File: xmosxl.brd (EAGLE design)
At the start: 130 x 85 mm, 139 parts, among them IC1 74LVC1T45W6-7, IC2 74LVC1T45W6-7, IC3 74LVC1T45W6-7, IC4 74LVC1T45W6-7, IC5 74LVC1T45W6-7, IC6 74ALVC164245DGG_11, IC7 74ALVC164245DGG_11, IC8 74LVC1T45W6-7, IC9 74LVC1T45W6-7, U1 24 MHz Osc. (F535L-24)

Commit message: Dd the link resistors
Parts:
- added R31, R32, R33, R34, R35: 33R, rcl:R0201
- moved R28 6.71 mm to (82.0, 52.5), turned to 180 degrees
- moved R16 6.40 mm to (79.0, 46.5)
- moved R17 6.02 mm to (77.5, 46.5)
- moved C39 1.50 mm to (67.0, 46.5)
- moved R24 1.00 mm to (53.5, 68.5)
- moved C27 0.50 mm to (65.0, 46.5)
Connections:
- new net N$27: R31.1, XMOS.N2
- new net N$28: R32.1, XMOS.P2
- new net N$29: R34.1, XMOS.R1
- new net N$30: R35.1, XMOS.R2
- net +5V: no longer JP1.13
- net RX0: no longer JP1.5
- net RX1: now also JP1.5; no longer JP1.9
- net RX2: now also JP1.9
- net RX3: now also JP1.13
- net RX4: now also R33.1
- net TX0: now also R31.2
- net TX1: now also R32.2
- net TX2: now also R33.2
- net TX3: now also R34.2
- net TX4: now also R35.2

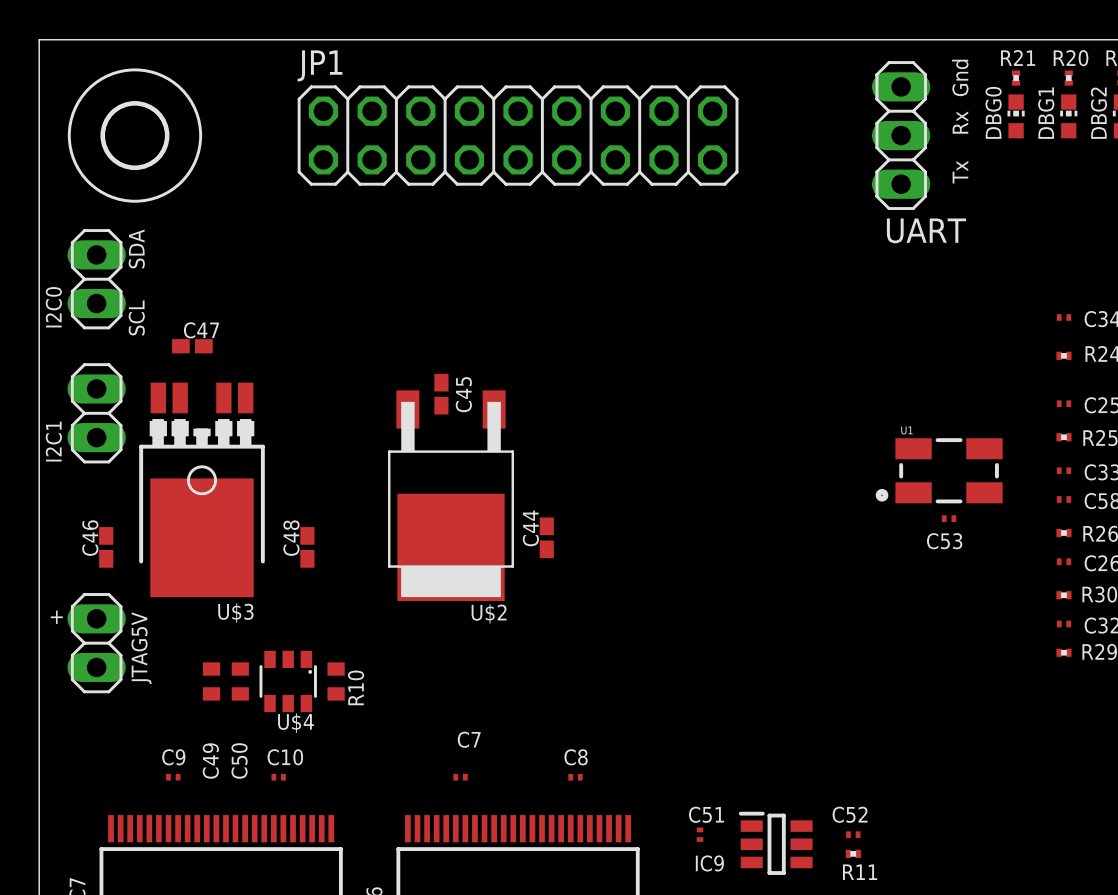
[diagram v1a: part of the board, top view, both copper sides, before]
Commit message: Board circuit-complete. Decided to ditch the SPI expansion.
Need to set signal classes and routing hints
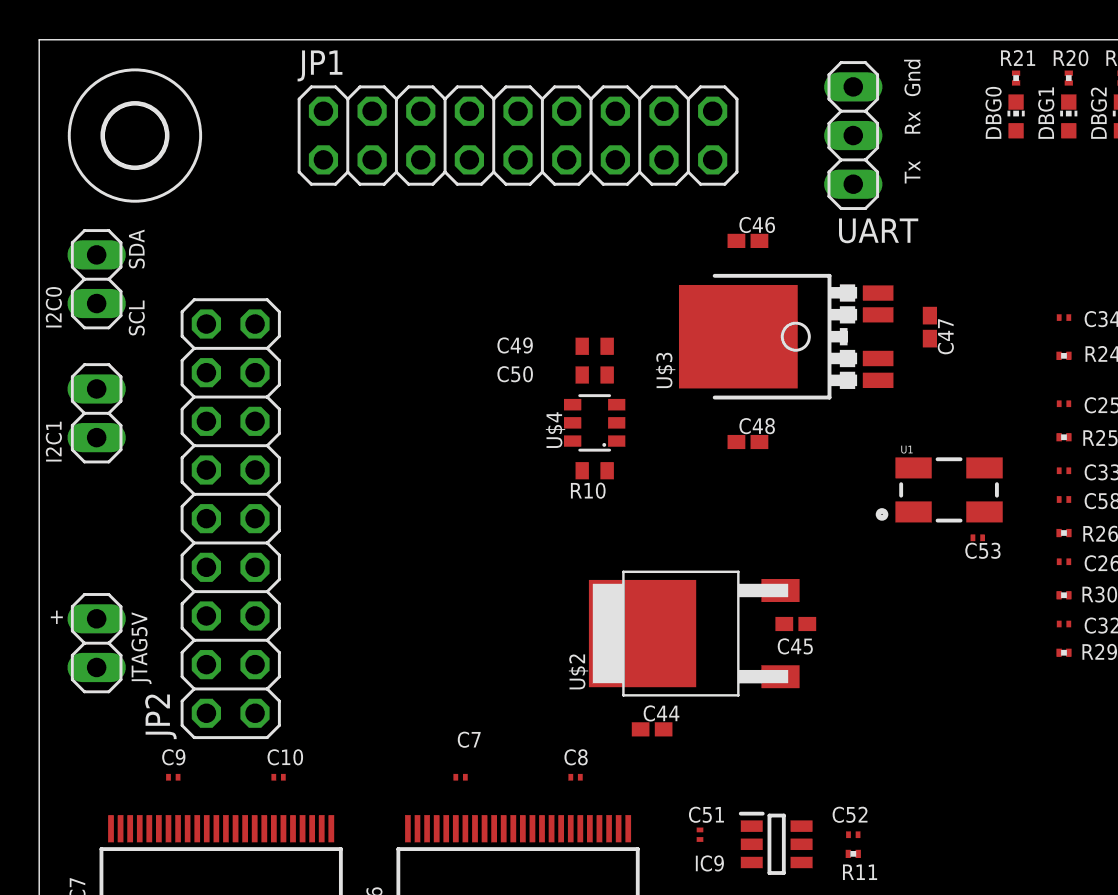
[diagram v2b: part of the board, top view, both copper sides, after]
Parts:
- added JP2: (no value), pinhead:2X09
- moved C47 38.5 mm to (46.5, 70.0), turned to 270 degrees
- moved C46 37.1 mm to (37.0, 74.5), turned to 0 degrees
- moved U$3 31.5 mm to (39.0, 69.5), turned to 90 degrees
- moved C49 26.6 mm to (29.0, 69.0), turned to 0 degrees
- moved C50 24.5 mm to (29.0, 67.5), turned to 0 degrees
- moved C48 23.6 mm to (37.0, 64.0), turned to 0 degrees
- moved C45 22.1 mm to (39.5, 54.5), turned to 0 degrees
- moved U$4 20.9 mm to (29.0, 65.0), turned to 90 degrees
- moved R10 17.4 mm to (29.0, 62.5), turned to 180 degrees
- moved C44 11.4 mm to (32.0, 49.0), turned to 0 degrees
- moved U$2 11.0 mm to (31.5, 54.0), turned to 90 degrees
- moved UART 2.50 mm to (42.5, 80.0)
- moved C53 1.80 mm to (49.0, 59.0)
- moved U1 1.00 mm to (47.5, 61.5)
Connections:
- new net XPND_CTRL0: JP2.3, XMOS.D19
- new net XPND_CTRL1: JP2.5, XMOS.D20
- new net XPND_CTRL2: JP2.7, XMOS.C13
- new net XPND_CTRL3: JP2.9, XMOS.D13
- new net XPND_CTRL4: JP2.11, XMOS.AA12
- new net XPND_CTRL5: JP2.13, XMOS.Y15
- new net XPND_CTRL6: JP2.15, XMOS.Y19
- new net XPND_DATA0: JP2.2, XMOS.U21
- new net XPND_DATA1: JP2.4, XMOS.T21
- new net XPND_DATA2: JP2.6, XMOS.R20
- new net XPND_DATA3: JP2.8, XMOS.R21
- new net XPND_DATA4: JP2.10, XMOS.P20
- new net XPND_DATA5: JP2.12, XMOS.P21
- new net XPND_DATA6: JP2.14, XMOS.E20
- new net XPND_DATA7: JP2.16, XMOS.E21
- net +3V3: now also SLOT1.B16, SLOT2.B17, SLOT3.B16, SLOT3.B17, SLOT4.B18, SLOT5.B16, SLOT5.B18; no longer JP1.11, JP1.12
- net +5V: now also JP1.3, JP1.4, JP2.1, SLOT1.A1, SLOT1.A2, SLOT1.B1, SLOT1.B2, SLOT2.A1, SLOT2.A2, SLOT2.B1, SLOT2.B2, SLOT3.A1, SLOT3.A2, SLOT3.B1, SLOT3.B2, SLOT4.A1, SLOT4.A2, SLOT4.B1, SLOT4.B2, SLOT5.A1, SLOT5.A2, SLOT5.B1, SLOT5.B2
- net GND: now also JP1.11, JP1.12, JP1.15, JP1.16, JP2.17, JP2.18, SLOT1.B17, SLOT1.B18, SLOT1.B19, SLOT1.B20, SLOT1.B21, SLOT1.B22, SLOT1.B23, SLOT1.B24, SLOT1.B25, SLOT1.B26, SLOT1.B27, SLOT1.B28, SLOT1.B29, SLOT1.B30, SLOT1.B31, SLOT1.B32, SLOT2.B16, SLOT2.B18, SLOT2.B19, SLOT2.B20, SLOT2.B21, SLOT2.B22, SLOT2.B23, SLOT2.B24, SLOT2.B25, SLOT2.B26, SLOT2.B27, SLOT2.B28, SLOT2.B29, SLOT2.B30, SLOT2.B31, SLOT2.B32, SLOT3.B18, SLOT3.B19, SLOT3.B20, SLOT3.B21, SLOT3.B22, SLOT3.B23, SLOT3.B24, SLOT3.B25, SLOT3.B26, SLOT3.B27, SLOT3.B28, SLOT3.B29, SLOT3.B30, SLOT3.B31, SLOT3.B32, SLOT4.B16, SLOT4.B17, SLOT4.B19, SLOT4.B20, SLOT4.B21, SLOT4.B22, SLOT4.B23, SLOT4.B24, SLOT4.B25, SLOT4.B26, SLOT4.B27, SLOT4.B28, SLOT4.B29, SLOT4.B30, SLOT4.B31, SLOT4.B32, SLOT5.B17, SLOT5.B19, SLOT5.B20, SLOT5.B21, SLOT5.B22, SLOT5.B23, SLOT5.B24, SLOT5.B25, SLOT5.B26, SLOT5.B27, SLOT5.B28, SLOT5.B29, SLOT5.B30, SLOT5.B31, SLOT5.B32; no longer JP1.3, JP1.4
- net SBUS_A0: now also SLOT1.A3, SLOT2.A3, SLOT3.A3, SLOT4.A3, SLOT5.A3
- net SBUS_A1: now also SLOT1.A4, SLOT2.A4, SLOT3.A4, SLOT4.A4, SLOT5.A4
- net SBUS_A10: now also SLOT1.A13, SLOT2.A13, SLOT3.A13, SLOT4.A13, SLOT5.A13
- net SBUS_A11: now also SLOT1.A14, SLOT2.A14, SLOT3.A14, SLOT4.A14, SLOT5.A14
- net SBUS_A12: now also SLOT1.A15, SLOT2.A15, SLOT3.A15, SLOT4.A15, SLOT5.A15
- net SBUS_A13: now also SLOT1.A16, SLOT2.A16, SLOT3.A16, SLOT4.A16, SLOT5.A16
- net SBUS_A14: now also SLOT1.A17, SLOT2.A17, SLOT3.A17, SLOT4.A17, SLOT5.A17
- net SBUS_A15: now also SLOT1.A18, SLOT2.A18, SLOT3.A18, SLOT4.A18, SLOT5.A18
- net SBUS_A2: now also SLOT1.A5, SLOT2.A5, SLOT3.A5, SLOT4.A5, SLOT5.A5
- net SBUS_A3: now also SLOT1.A6, SLOT2.A6, SLOT3.A6, SLOT4.A6, SLOT5.A6
- net SBUS_A4: now also SLOT1.A7, SLOT2.A7, SLOT3.A7, SLOT4.A7, SLOT5.A7
- net SBUS_A5: now also SLOT1.A8, SLOT2.A8, SLOT3.A8, SLOT4.A8, SLOT5.A8
- net SBUS_A6: now also SLOT1.A9, SLOT2.A9, SLOT3.A9, SLOT4.A9, SLOT5.A9
- net SBUS_A7: now also SLOT1.A10, SLOT2.A10, SLOT3.A10, SLOT4.A10, SLOT5.A10
- net SBUS_A8: now also SLOT1.A11, SLOT2.A11, SLOT3.A11, SLOT4.A11, SLOT5.A11
- net SBUS_A9: now also SLOT1.A12, SLOT2.A12, SLOT3.A12, SLOT4.A12, SLOT5.A12
- net SBUS_CLK: now also SLOT1.A19, SLOT2.A19, SLOT3.A19, SLOT4.A19, SLOT5.A19
- net SBUS_D0: now also SLOT1.A20, SLOT2.A20, SLOT3.A20, SLOT4.A20, SLOT5.A20
- net SBUS_D1: now also SLOT1.A21, SLOT2.A21, SLOT3.A21, SLOT4.A21, SLOT5.A21
- net SBUS_D2: now also SLOT1.A22, SLOT2.A22, SLOT3.A22, SLOT4.A22, SLOT5.A22
- net SBUS_D3: now also SLOT1.A23, SLOT2.A23, SLOT3.A23, SLOT4.A23, SLOT5.A23
- net SBUS_D4: now also SLOT1.A24, SLOT2.A24, SLOT3.A24, SLOT4.A24, SLOT5.A24
- net SBUS_D5: now also SLOT1.A25, SLOT2.A25, SLOT3.A25, SLOT4.A25, SLOT5.A25
- net SBUS_D6: now also SLOT1.A26, SLOT2.A26, SLOT3.A26, SLOT4.A26, SLOT5.A26
- net SBUS_D7: now also SLOT1.A27, SLOT2.A27, SLOT3.A27, SLOT4.A27, SLOT5.A27
- net SBUS_FLG0: now also SLOT1.A28, SLOT2.A28, SLOT3.A28, SLOT4.A28, SLOT5.A28
- net SBUS_FLG1: now also SLOT1.A29, SLOT2.A29, SLOT3.A29, SLOT4.A29, SLOT5.A29
- net SBUS_FLG2: now also SLOT1.A30, SLOT2.A30, SLOT3.A30, SLOT4.A30, SLOT5.A30
- net SBUS_FLG3: now also SLOT1.A31, SLOT2.A31, SLOT3.A31, SLOT4.A31, SLOT5.A31
- net SBUS_FLG4: now also SLOT1.A32, SLOT2.A32, SLOT3.A32, SLOT4.A32, SLOT5.A32
- net SPI_BOPT0: now also SLOT1.B3, SLOT2.B3, SLOT3.B3, SLOT4.B3, SLOT5.B3
- net SPI_BOPT1: now also SLOT1.B4, SLOT2.B4, SLOT3.B4, SLOT4.B4, SLOT5.B4
- net SPI_BOPT2: now also SLOT1.B5, SLOT2.B5, SLOT3.B5, SLOT4.B5, SLOT5.B5
- net SPI_BOPT3: now also SLOT1.B6, SLOT2.B6, SLOT3.B6, SLOT4.B6, SLOT5.B6
- net SPI_BSEL0: now also SLOT1.B7, SLOT2.B7, SLOT3.B7, SLOT4.B7, SLOT5.B7
- net SPI_BSEL1: now also SLOT1.B8, SLOT2.B8, SLOT3.B8, SLOT4.B8, SLOT5.B8
- net SPI_BSEL2: now also SLOT1.B9, SLOT2.B9, SLOT3.B9, SLOT4.B9, SLOT5.B9
- net SPI_BSEL3: now also SLOT1.B10, SLOT2.B10, SLOT3.B10, SLOT4.B10, SLOT5.B10
- net SPI_CLK0: now also SLOT1.B11, SLOT2.B11, SLOT3.B11, SLOT4.B11, SLOT5.B11
- net SPI_IRQ0: now also SLOT1.B12
- net SPI_IRQ1: now also SLOT2.B12
- net SPI_IRQ2: now also SLOT3.B12
- net SPI_IRQ3: now also SLOT4.B12
- net SPI_IRQ4: now also SLOT5.B12
- net SPI_MISO0: now also SLOT1.B13, SLOT2.B13, SLOT3.B13, SLOT4.B13, SLOT5.B13
- net SPI_MOSI0: now also SLOT1.B14, SLOT2.B14, SLOT3.B14, SLOT4.B14, SLOT5.B14
- net SPI_SS0: now also SLOT1.B15
- net SPI_SS1: now also SLOT2.B15
- net SPI_SS2: now also SLOT3.B15
- net SPI_SS3: now also SLOT4.B15
- net SPI_SS4: now also SLOT5.B15
- net VDD: no longer JP1.15, JP1.16
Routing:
- added copper zone on layer 15, net +3V3
- added copper zone on layer 15, net +5V
- added copper zone on layer 2, net GND
- added copper zone on layer 3, net VDD

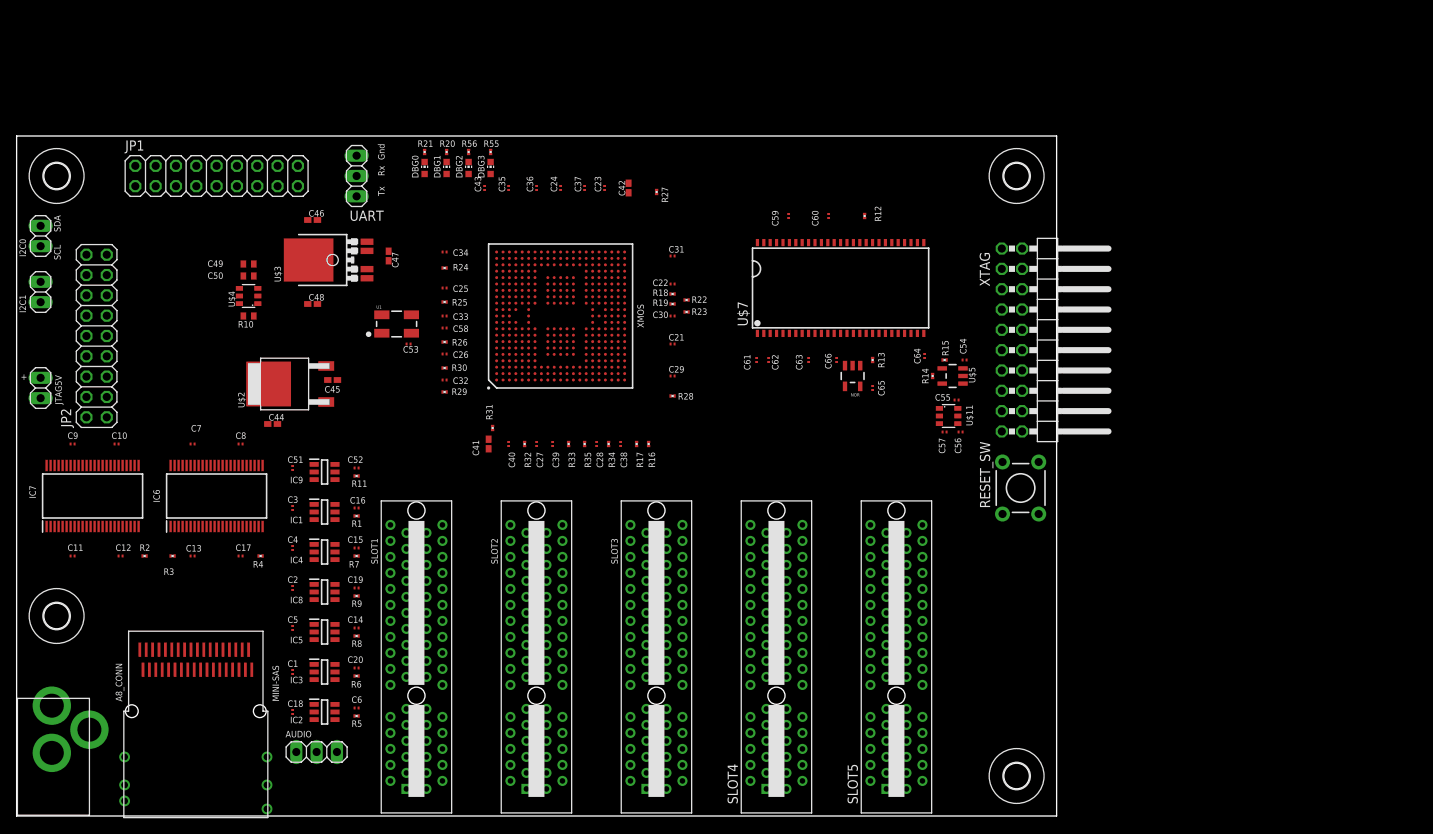
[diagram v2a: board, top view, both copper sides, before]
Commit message: Add some power rail stuff
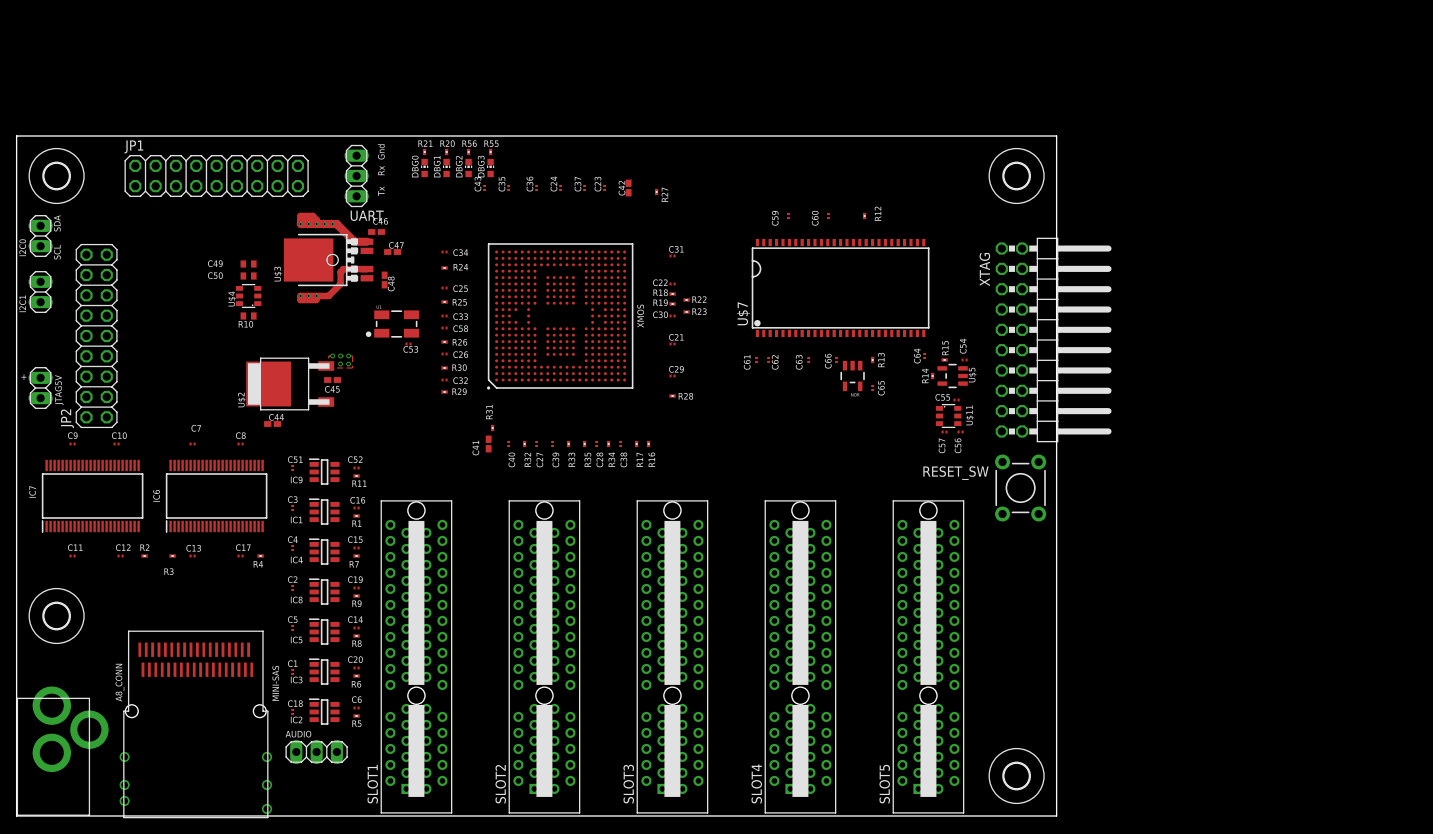
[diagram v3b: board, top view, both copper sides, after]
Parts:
- moved C48 9.49 mm to (46.0, 67.0), turned to 270 degrees
- moved C46 8.14 mm to (45.0, 73.0)
- moved SLOT5 4.00 mm to (114.0, 15.0)
- moved SLOT4 3.00 mm to (98.0, 15.0)
- moved SLOT3 2.00 mm to (82.0, 15.0)
- moved SLOT2 1.00 mm to (66.0, 15.0)
- moved C47 0.71 mm to (47.0, 70.5), turned to 0 degrees
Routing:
- net +5V: track 0.00 -> 27.7 mm, vias 0 -> 8
- added copper zone on layer 1, net +3V3
